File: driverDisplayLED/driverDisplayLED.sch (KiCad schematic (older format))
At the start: 70 parts, among them J1 Conn_01x12_Male, J10 Conn_01x12_Male, J11 Conn_01x12_Male, J12 Conn_01x12_Male, J13 Conn_01x12_Male, J14 Conn_01x12_Male, J15 Conn_01x12_Male, J16 Conn_01x12_Male, J17 Conn_01x12_Male, J18 Conn_02x08_Counter_Clockwise, J2 Conn_01x12_Male, J3 Conn_01x12_Male, J4 Conn_02x08_Counter_Clockwise, J5 Conn_01x12_Male, J6 Conn_01x12_Male, J7 Conn_01x12_Male, J8 Conn_01x12_Male, J9 Conn_01x12_Male, Q1 FDS4953, Q2 FDS4953, Q3 FDS4953, Q4 FDS4953, Q5 FDS4953, Q6 FDS4953, Q7 FDS4953, Q8 FDS4953, U1 74HC245, U10 74HC595, U11 74HC595, U12 74HC595, U13 74HC595, U2 74HC595, U3 74HC595, U4 74HC245, U5 74HC138D, U6 74HC04, U7 74HC595, U8 74HC595, U9 74HC138D

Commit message: place components, continued
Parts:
- J1, J10, J11, J12, J13, J14, J15, J16, J17, J2, J3, J5, J6, J7, J8, J9: footprint Connector_PinHeader_1.00mm:PinHeader_1x12_P1.00mm_Vertical -> Connector_PinSocket_2.54mm:PinSocket_1x12_P2.54mm_Vertical
- U1, U4: footprint Package_SO:HSOP-20-1EP_11.0x15.9mm_P1.27mm_SlugDown_ThermalVias -> Package_SO:SO-20-1EP_7.52x12.825mm_P1.27mm_EP6.045x12.09mm_Mask3.56x4.47mm
- U10, U11, U12, U13, U2, U3, U7, U8: footprint Package_SO:HTSSOP-16-1EP_4.4x5mm_P0.65mm_EP3.4x5mm -> Package_SO:SO-16_5.3x10.2mm_P1.27mm
- U5, U9: footprint Package_SO:TSSOP-16_4.4x5mm_P0.65mm -> Package_SO:SO-16_5.3x10.2mm_P1.27mm

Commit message: ERC with no errors. Onlly warnings
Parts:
- removed C10, C12, C13, C9: C, Capacitor_SMD:CP_Elec_3x5.3, symbol Device:C
- removed RN1, RN3, RN4, RN5: R_Network04, Resistor_THT:R_Array_SIP4, symbol Device:R_Network04
- removed U10, U11, U12, U13: 74HC595, Package_SO:SO-16_5.3x10.2mm_P1.27mm, symbol 74xx:74HC595
- added J19: Conn_01x02_Female, symbol Connector:Conn_01x02_Female
- added RN6, RN7, RN8, RN9: 50, Resistor_THT:R_Array_SIP4, symbol Device:R_Network04
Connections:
- net labels added: H1a, H1b, H2a, H2b, H3a, H3b, H4a, H4b, H5a, H5b, H6a, H6b, H7a, H7b, H8a, H8b, L1G1, L1G2, L1G3, L1G4, L1G5, L1G6, L1G7, L1G8, L1R1, L1R2, L1R3, L1R4, L1R5, L1R6, L1R7, L1R8, L2G1, L2G2, L2G3, L2G4, L2G5, L2G6, L2G7, L2G8, L3G1, L3G3, L3G4, L3G5, L3G6, L3G7, L3G8, L3R1, L3R2, L3R3, L3R4, L3R5, L3R6, L3R7, L3R8, L4G1, L4G2, L4G3, L4G4, L4G5, L4G6, L4G7, L4G8, L5G1, L5G2, L5G3, L5G4, L5G5, L5G6, L5G7, L5G8, L5R1, L5R2, L5R3, L5R4, L5R5, L5R6, L5R7, L5R8, L6G1, L6G2, L6G3, L6G4, L6G5, L6G6, L6G7, L6G8, L7G1, L7G2, L7G3, L7G4, L7G5, L7G6, L7G7, L7G8, L7R1, L7R2, L7R3, L7R4, L7R5, L7R6, L7R7, L7R8, L8G1, L8G2, L8G3, L8G4, L8G5, L8G6, L8G7, L8G8, LRG2, Y0-G2a, Y0-G2b, Y1-G1a, Y1-G1b, Y2-G2a, Y2-G2b, Y3-G1a, Y3-G1b, Y4-G2a, Y4-G2b, Y5-G1a, Y5-G1b, Y6-G2a, Y6-G2b, Y7-G1a, Y7-G1b
- net labels removed: D1-H2, D1-H4, D2-H1, D2-H3, G1, G2, G3, G4, G5, G6, G7, G8, H1, H2, H3, H4, H5, H6, H7, H8, R1, R2, R3, R4, R5, R6, R7, R8, Y0-G2, Y1-G1, Y2-G2, Y3-G1, Y4-G2, Y5-G1, Y6-G2, Y7-G1
- wire segments 724 -> 654
- no-connect marks 5 -> 12
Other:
- moved on the sheet: C1, C11, C2, C3, C4, C5, C6, C7, C8, D1, D2, J1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

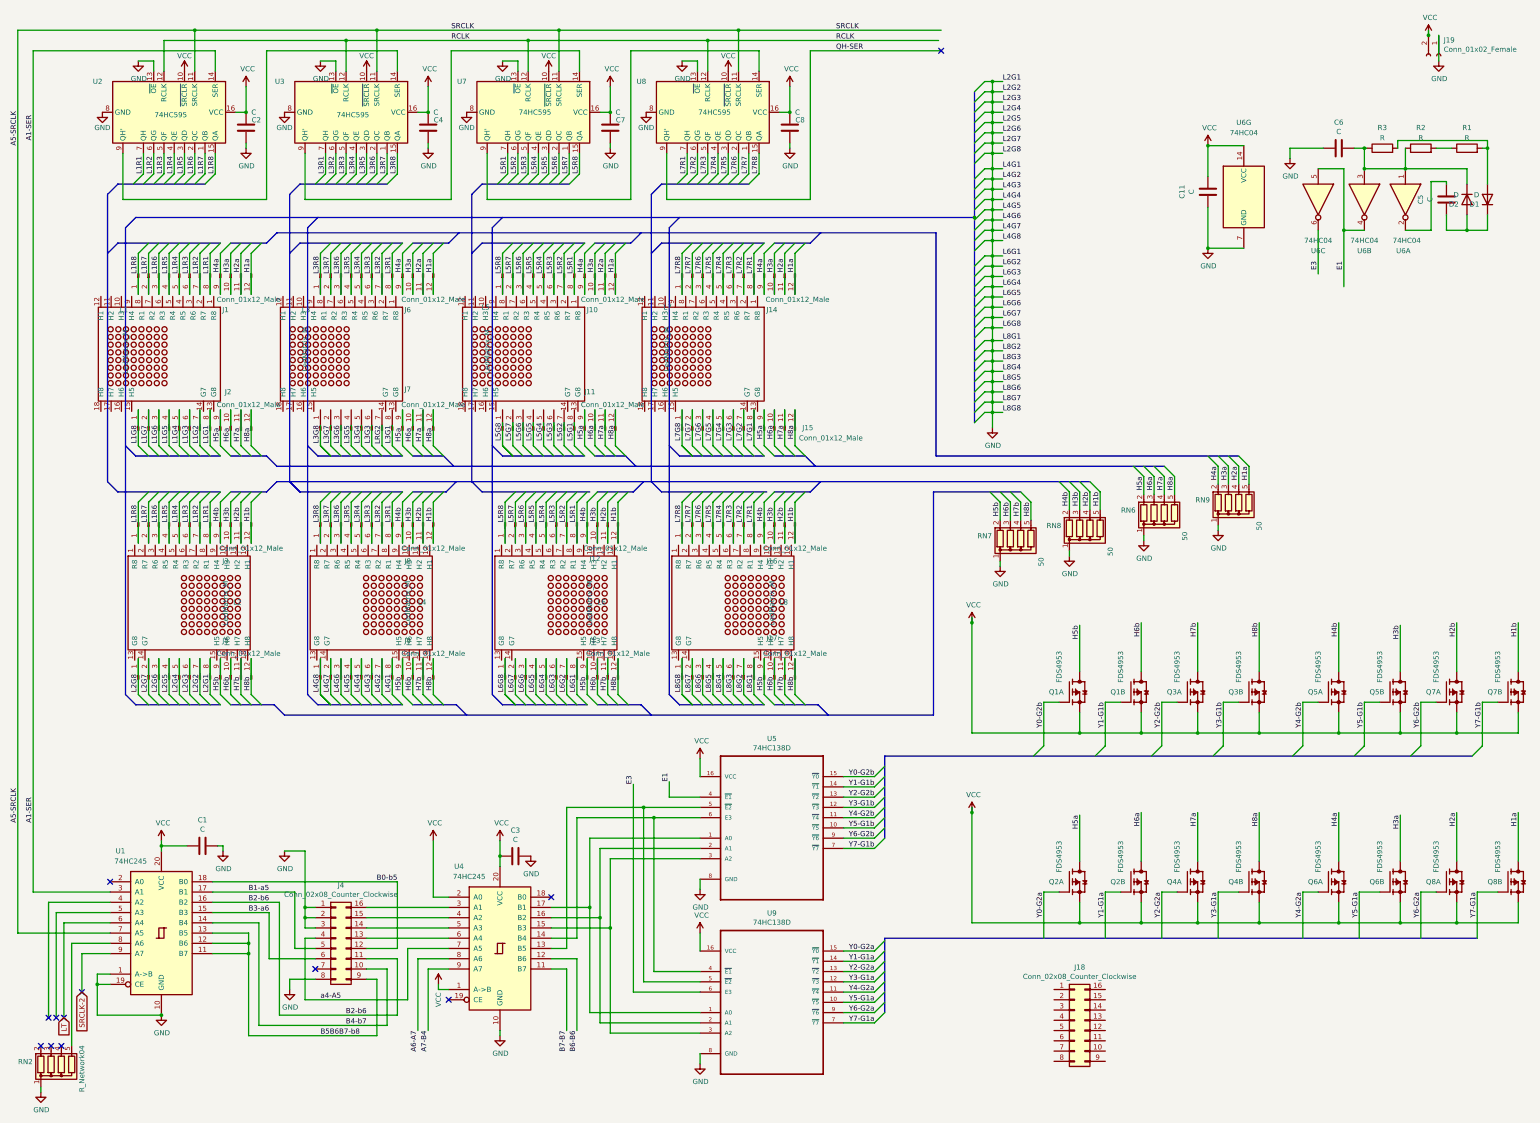
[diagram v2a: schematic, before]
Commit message: agrego textos. Listo para revisión esquemático
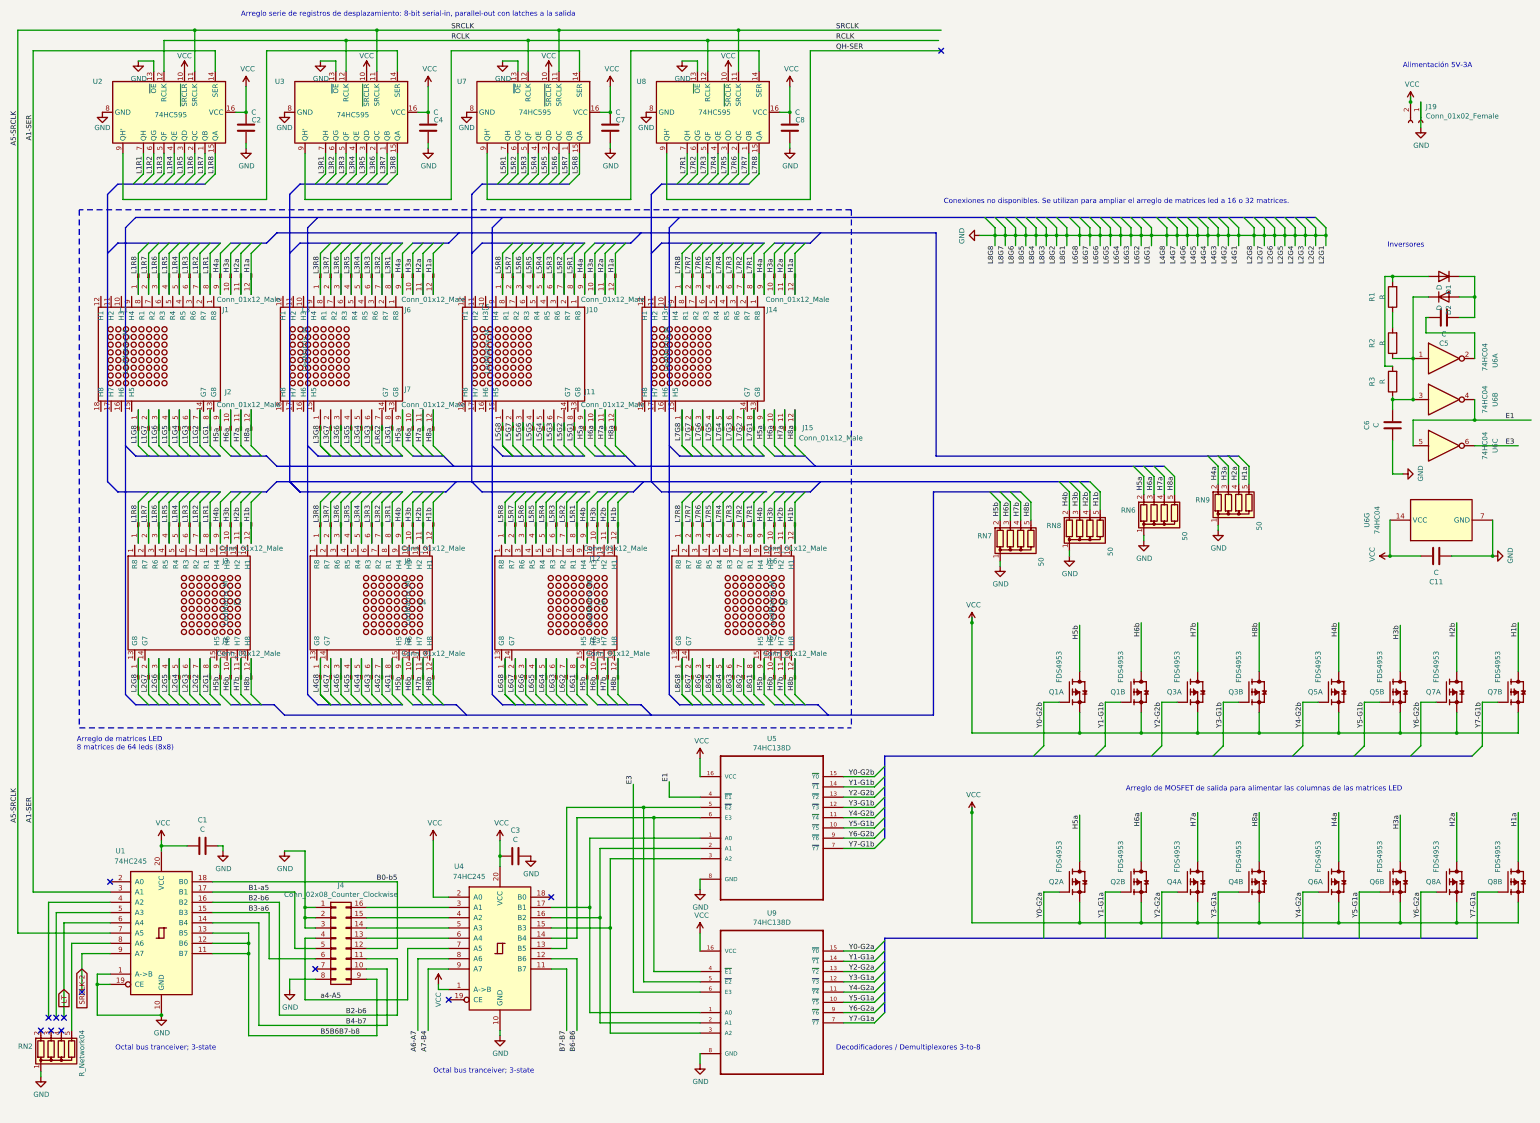
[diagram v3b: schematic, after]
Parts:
- removed J18: Conn_02x08_Counter_Clockwise, Connector_PinHeader_2.54mm:PinHeader_2x08_P2.54mm_Vertical, symbol Connector_Generic:Conn_02x08_Counter_Clockwise
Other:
- note added: "Alimentación 5V-3A\n"
- note added: "Arreglo de MOSFET de salida para alimentar las columnas de las matrices LED\n"
- note added: "Arreglo de matrices LED\n8 matrices de 64 leds (8x8)\n"
- note added: "Arreglo serie de registros de desplazamiento: 8-bit serial-in, parallel-out con latches a la salida"
- note added: "Conexiones no disponibles. Se utilizan para ampliar el arreglo de matrices led a 16 o 32 matrices."
- note added: "Decodificadores / Demultiplexores 3-to-8\n"
- note added: "Inversores"
- note added: "Octal bus tranceiver; 3-state\n"
- moved on the sheet: C11, C5, C6, D1, D2, J19, R1, R2, R3, RN2, U6A, U6B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

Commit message: place and route
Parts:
- added H1, H2, H3, H4, H5, H6: MountingHole, MountingHole:MountingHole_2.7mm_M2.5_ISO14580, symbol Mechanical:MountingHole
- J4: symbol Connector_Generic:Conn_02x08_Counter_Clockwise -> Connector_Generic:Conn_02x08_Odd_Even
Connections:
- net B0-b5: now also J4.10 (Pin_10); no longer J4.12 (Pin_12)
- net B1-a5: now also J4.9 (Pin_9); no longer J4.5 (Pin_5)
- net B2-b6: now also J4.12 (Pin_12); no longer J4.11 (Pin_11)
- net B3-a6: now also J4.11 (Pin_11); no longer J4.6 (Pin_6)
- net B4-b7: now also J4.14 (Pin_14); no longer J4.10 (Pin_10)
- net B5B6B7-b8: now also J4.16 (Pin_16); no longer J4.9 (Pin_9)
- net GND: now also J4.15 (Pin_15), J4.5 (Pin_5); no longer J4.2 (Pin_2), J4.8 (Pin_8)
- net a4-A5: now also J4.7 (Pin_7); no longer J4.4 (Pin_4)
- net at U4.3 (A1): now also J4.2 (Pin_2); no longer J4.16 (Pin_16)
- net at U4.4 (A2): now also J4.4 (Pin_4); no longer J4.15 (Pin_15)
- net at U4.5 (A3): now also J4.6 (Pin_6); no longer J4.14 (Pin_14)
- net at U4.6 (A4): now also J4.8 (Pin_8); no longer J4.13 (Pin_13)
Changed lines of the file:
@@
 	4800 10125 4800 10175
 $Comp
-L Connector_Generic:Conn_02x08_Counter_Clockwise J4
+L Connector_Generic:Conn_02x08_Odd_Even J4
 U 1 1 5F72EC68
 P 3800 9675
 F 0 "J4" H 3850 10192 50  0000 C CNN
 F 1 "Conn_02x08_Counter_Clockwise" H 3850 10101 50  0000 C CNN
-F 2 "Connector_PinHeader_2.54mm:PinHeader_2x08_P2.54mm_Vertical" H 3800 9675 50  0001 C CNN
+F 2 "Connector_PinHeader_2.54mm:PinHeader_2x08_P2.54mm_Vertical" V 3800 9675 50  0001 C CNN
 F 3 "~" H 3800 9675 50  0001 C CNN
 	1    3800 9675
@@
 $EndComp
 Wire Wire Line
-	14375 1775 14375 1525
+	14375 1775 14375 1725
 Text Label 7975 4675 3    50   ~ 0
 H5a
@@
 Text Notes 9725 2525 0    50   ~ 0
 Conexiones no disponibles. Se utilizan para ampliar el arreglo de matrices led a 16 o 32 matrices.
+Text Notes 14200 1200 0    50   ~ 0
+Alimentación 5V-3A\n
+$Comp
+L power:PWR_FLAG #FLG0101
+U 1 1 5F905A82
+P 14150 1525
+F 0 "#FLG0101" H 14150 1600 50  0001 C CNN
+F 1 "PWR_FLAG" V 14150 1675 50  0000 L CNN
+F 2 "" H 14150 1525 50  0001 C CNN
+F 3 "~" H 14150 1525 50  0001 C CNN
+	1    14150 1525
+	0    -1   -1   0
+$EndComp
+$Comp
+L power:GNDPWR #PWR0112
+U 1 1 5F906B75
+P 14625 1900
+F 0 "#PWR0112" H 14625 1700 50  0001 C CNN
+F 1 "GNDPWR" H 14629 1746 50  0000 C CNN
+F 2 "" H 14625 1850 50  0001 C CNN
+F 3 "" H 14625 1850 50  0001 C CNN
+	1    14625 1900
+	1    0    0    -1
+$EndComp
+Wire Wire Line
+	14625 1900 14625 1725
+Wire Wire Line
+	14625 1725 14375 1725
+Connection ~ 14375 1725
+Wire Wire Line
+	14375 1725 14375 1525
+Wire Wire Line
+	14150 1525 14150 1675
+Wire Wire Line
+	14150 1675 14275 1675
+Wire Wire Line
+	14275 1525 14275 1675
+$Comp
+L Mechanical:MountingHole H1
+U 1 1 5FC4D813
+P 10650 3775
+F 0 "H1" H 10750 3821 50  0000 L CNN
+F 1 "MountingHole" H 10750 3730 50  0000 L CNN
+F 2 "MountingHole:MountingHole_2.7mm_M2.5_ISO14580" H 10650 3775 50  0001 C CNN
+F 3 "~" H 10650 3775 50  0001 C CNN
+	1    10650 3775
+	1    0    0    -1
+$EndComp
+$Comp
+L Mechanical:MountingHole H2
+U 1 1 5FC64412
+P 10650 4100
+F 0 "H2" H 10750 4146 50  0000 L CNN
+F 1 "MountingHole" H 10750 4055 50  0000 L CNN
+F 2 "MountingHole:MountingHole_2.7mm_M2.5_ISO14580" H 10650 4100 50  0001 C CNN
+F 3 "~" H 10650 4100 50  0001 C CNN
+	1    10650 4100
+	1    0    0    -1
+$EndComp
+$Comp
+L Mechanical:MountingHole H3
+U 1 1 5FC6A707
+P 11475 3775
+F 0 "H3" H 11575 3821 50  0000 L CNN
+F 1 "MountingHole" H 11575 3730 50  0000 L CNN
+F 2 "MountingHole:MountingHole_2.7mm_M2.5_ISO14580" H 11475 3775 50  0001 C CNN
+F 3 "~" H 11475 3775 50  0001 C CNN
+	1    11475 3775
+	1    0    0    -1
+$EndComp
+$Comp
+L Mechanical:MountingHole H4
+U 1 1 5FC6A70D
+P 11475 4100
+F 0 "H4" H 11575 4146 50  0000 L CNN
+F 1 "MountingHole" H 11575 4055 50  0000 L CNN
+F 2 "MountingHole:MountingHole_2.7mm_M2.5_ISO14580" H 11475 4100 50  0001 C CNN
+F 3 "~" H 11475 4100 50  0001 C CNN
+	1    11475 4100
+	1    0    0    -1
+$EndComp
+$Comp
+L Mechanical:MountingHole H5
+U 1 1 5FCFED76
+P 12275 3775
+F 0 "H5" H 12375 3821 50  0000 L CNN
+F 1 "MountingHole" H 12375 3730 50  0000 L CNN
+F 2 "MountingHole:MountingHole_2.7mm_M2.5_ISO14580" H 12275 3775 50  0001 C CNN
+F 3 "~" H 12275 3775 50  0001 C CNN
+	1    12275 3775
+	1    0    0    -1
+$EndComp
+$Comp
+L Mechanical:MountingHole H6
+U 1 1 5FCFED7C
+P 12275 4100
+F 0 "H6" H 12375 4146 50  0000 L CNN
+F 1 "MountingHole" H 12375 4055 50  0000 L CNN
+F 2 "MountingHole:MountingHole_2.7mm_M2.5_ISO14580" H 12275 4100 50  0001 C CNN
+F 3 "~" H 12275 4100 50  0001 C CNN
+	1    12275 4100
+	1    0    0    -1
+$EndComp
 Wire Bus Line
 	1575 2425 1575 5225
@@
 Wire Bus Line
 	1850 2650 13350 2650
-Text Notes 14200 1200 0    50   ~ 0
-Alimentación 5V-3A\n
 $EndSCHEMATC

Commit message: footprint matrix + vias primer bloque
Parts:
- J19: footprint (none) -> Connector_Phoenix_MC:PhoenixContact_MCV_1,5_2-GF-3.5_1x02_P3.50mm_Vertical_ThreadedFlange_MountHole
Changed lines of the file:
@@
 F 0 "J19" V 14221 1773 50  0000 L CNN
 F 1 "Conn_01x02_Female" V 14312 1773 50  0000 L CNN
-F 2 "" H 14375 1725 50  0001 C CNN
+F 2 "Connector_Phoenix_MC:PhoenixContact_MCV_1,5_2-GF-3.5_1x02_P3.50mm_Vertical_ThreadedFlange_MountHole" H 14375 1725 50  0001 C CNN
 F 3 "~" H 14375 1725 50  0001 C CNN
 	1    14375 1725

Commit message: Esquemático actualizado, encapsulados de capacitores actualizados, footprints de prueba de las matrices led, vias
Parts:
- removed C5, C6: C, Capacitor_SMD:CP_Elec_3x5.3, symbol Device:C
- removed D1, D2: D, Diode_SMD:D_0201_0603Metric, symbol Device:D
- removed R1, R2, R3: R, Resistor_SMD:R_0201_0603Metric, symbol Device:R
- removed unit 1 of U6
- removed unit 2 of U6
- removed unit 3 of U6
- added C? (x2): C, Capacitor_SMD:CP_Elec_3x5.3, symbol Device:C
- added D? (x2): D, Diode_SMD:D_0201_0603Metric, symbol Device:D
- added R? (x3): R, Resistor_SMD:R_0201_0603Metric, symbol Device:R
- added U? (x3): 74HC04, Package_SO:TSSOP-14_4.4x5mm_P0.65mm, symbol 74xx:74HC04
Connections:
- net E1: now also U?.4
- net E3: now also U?.6
- net GND: now also C?.2, D?.2 (A), R?.2, R?.2
- net at U1.8 (A6): now also RN2.2 (R1); no longer RN2.5 (R4)
- net at J4.2 (Pin_2), U4.3 (A1): now also R?.2
- new net: C?.1, D?.1 (K), R?.1, U?.3
- new net: R?.1, R?.1, U?.1
- new net: C?.1, U?.2
- new net: C?.2, D?.1 (K), D?.2 (A)
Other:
- moved on the sheet: C1, C11, C3, H1, H2, H3, H4, H5, H6, J19, J4, Q1A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
